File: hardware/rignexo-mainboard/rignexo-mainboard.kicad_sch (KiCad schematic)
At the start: 33 parts, among them J1 AudioJack3, J2 AudioJack3, K1 Relay_DPDT, Q1 MMBT3904, T1 PA0185NL, T2 PA0185NL, U2 RP2040_Zero

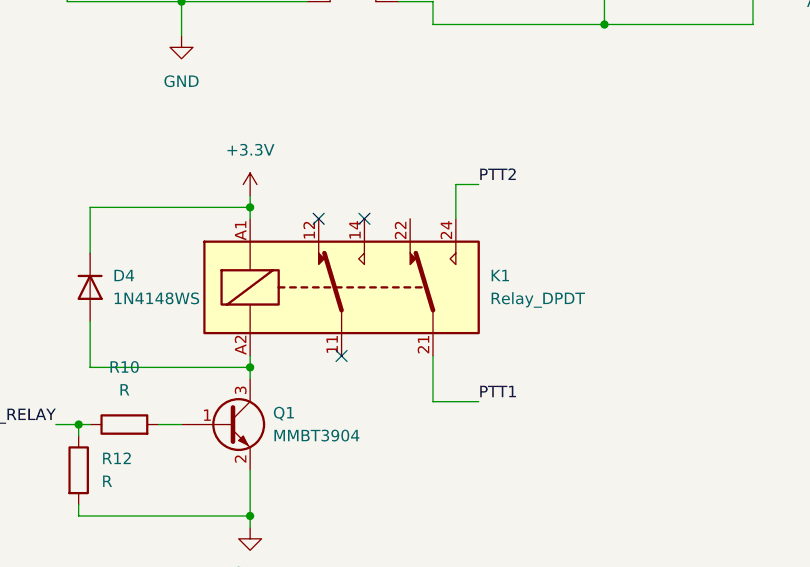
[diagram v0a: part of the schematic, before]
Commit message: Fix mainboard relay coil schematic and PCB routing.
Correct the relay coil wiring error in the schematic and update the board routing; remove outdated Gerber outputs generated from the faulty layout.
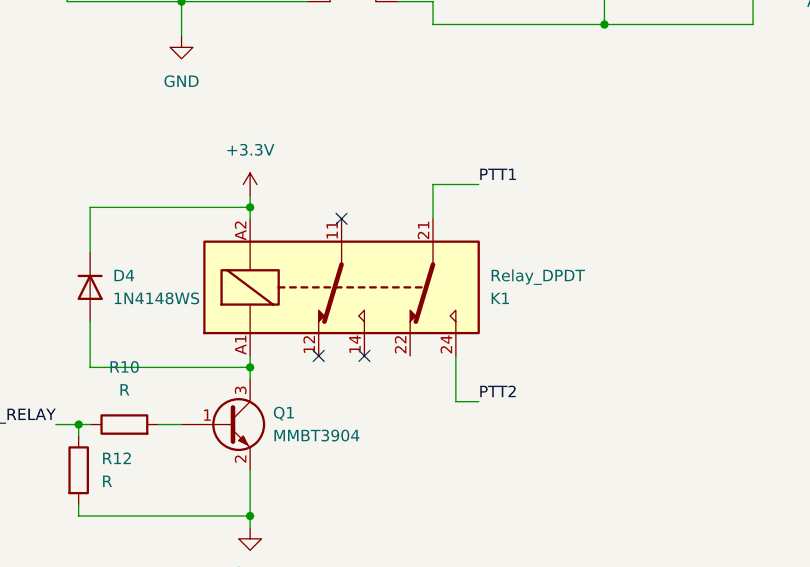
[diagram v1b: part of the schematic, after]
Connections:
- net +3.3V: now also K1.A2; no longer K1.A1
- net at D4.2 (A), Q1.3 (C): now also K1.A1; no longer K1.A2

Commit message: Update mainboard with mode switch and local footprints.
Add a project-local CustomPartsLocal library for the 3x4mm SMD
pushbutton, wire MODE_SWITCH/MODE_LED, and add solder jumpers so
K1 lines can stay independent. Update schematic and PCB routing
to match.
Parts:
- added JP1, JP2, JP3, JP4: SolderJumper_2_Open, Jumper:SolderJumper-2_P1.3mm_Open_RoundedPad1.0x1.5mm, symbol Jumper:SolderJumper_2_Open
- added R13: R, Resistor_SMD:R_0805_2012Metric_Pad1.20x1.40mm_HandSolder, symbol Device:R
- added SW1: SW_Push, CustomPartsLocal:SW_SMD_Push_3X4mm_2_pin, symbol Switch:SW_Push
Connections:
- net +3.3V: now also SW1.2; no longer R4.1
- net GND: now also R13.2
- net PTT1: now also JP1.1 (A), JP2.1 (A); no longer J2.R
- net PTT2: now also JP3.1 (A), JP4.1 (A); no longer J1.T
- net at J2.S, T2.4: now also JP2.2 (B)
- net at J1.S, RV1.1, T1.4: now also JP3.2 (B)
- net MODE_LED: now reaches U2.18 (GPIO0)
- net MODE_LED: now also R4.1
- net MODE_SWITCH: now reaches U2.8 (GPIO15)
- net MODE_SWITCH: now also R13.1, SW1.1
- new net: J1.T, JP4.2 (B)
- new net: J2.R, JP1.2 (B)
- no-connect marks 15 -> 13
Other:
- note added: "ALL LINES INDEPENDENT"
- note added: "K1 CONNECTOR"
- note added: "MODE LED"
- note added: "MODE SWITCH"
- note removed: "POWER ON LED"
- moved on the sheet: C1, D4, K1, Q1, R10, R12
